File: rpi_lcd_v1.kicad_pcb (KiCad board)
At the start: 2 copper layers, 43.5 x 53 mm, 21 parts, among them J1 RPI GPIO, P1 CONN_9

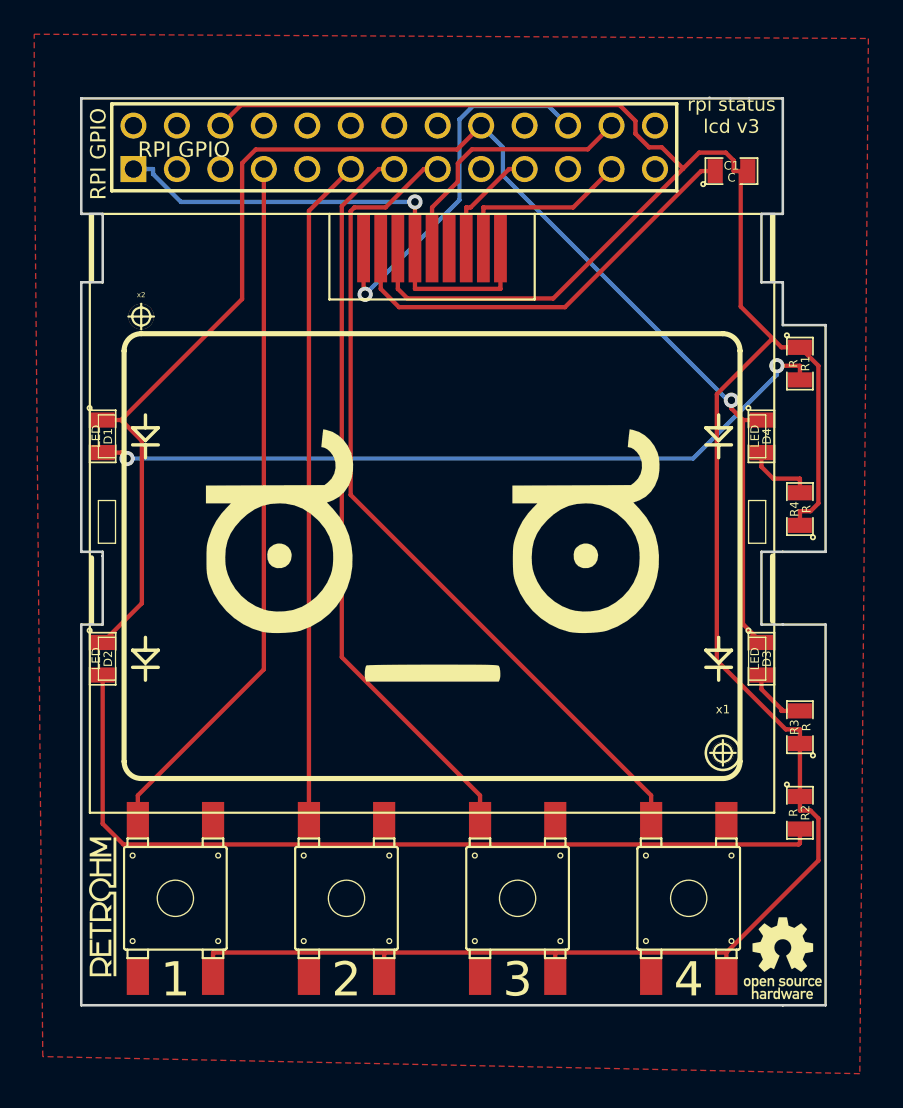
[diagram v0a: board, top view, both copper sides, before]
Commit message: Fixed d/c line, fixed LED orientation
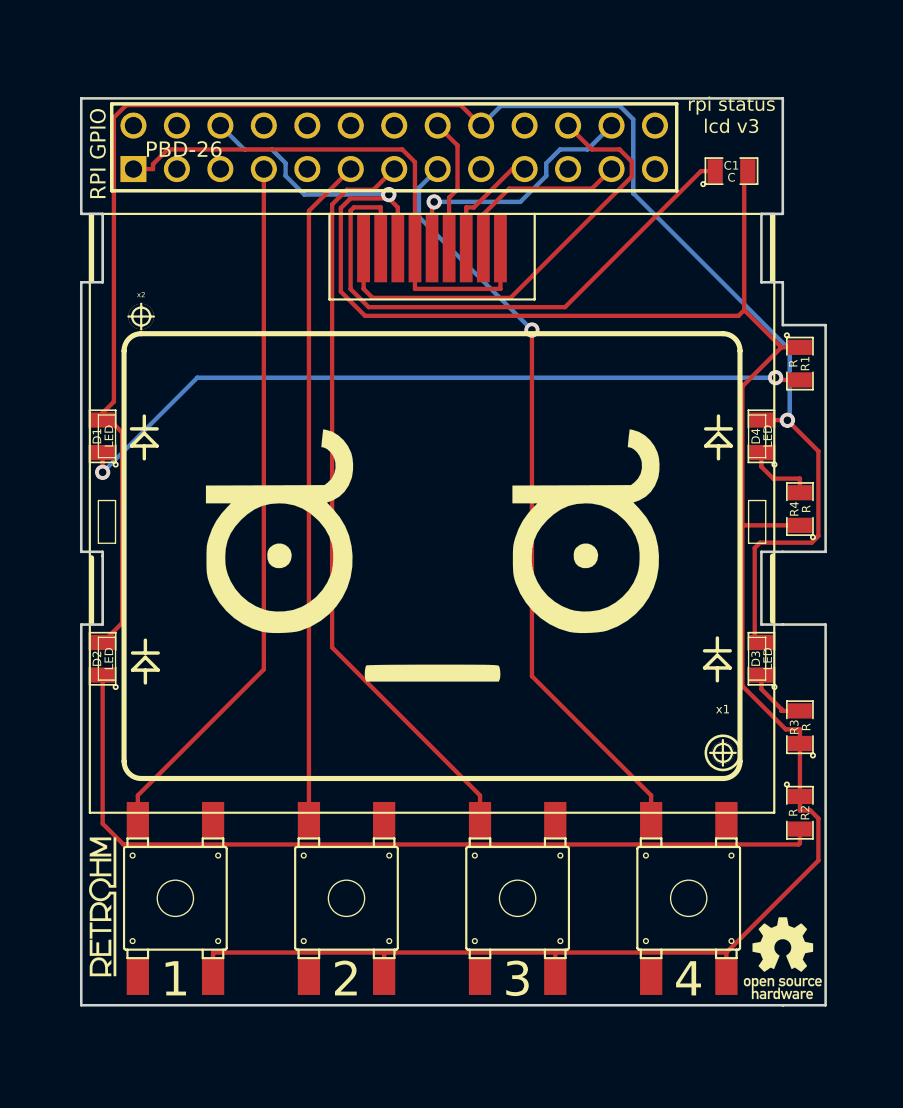
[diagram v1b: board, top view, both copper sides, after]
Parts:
- J1: value RPI GPIO -> PBD-26
- SW_1: value 1 -> FSM4JSMA-SMD
- SW_2: value 2 -> FSM4JSMA-SMD
- SW_3: value 3 -> FSM4JSMA-SMD
- SW_4: value 4 -> FSM4JSMA-SMD
- turned D1 to 90 degrees
- turned D2 to 90 degrees
- turned D3 to 90 degrees
- turned D4 to 90 degrees
- renumbered VAL to back_scaled
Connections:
- D1 pad 1: N-0000028 -> N-0000030
- D1 pad 2: N-0000031 -> N-0000027
- D2 pad 1: N-0000028 -> N-0000031
- D2 pad 2: N-0000032 -> N-0000027
- D3 pad 2: N-0000029 -> N-0000027
- D4 pad 1: N-0000028 -> N-0000029
- D4 pad 2: N-0000030 -> N-0000027
- J1 pad 10: (no net) -> N-0000018
- J1 pad 12: (no net) -> N-0000020
- J1 pad 14: (no net) -> N-0000013
- J1 pad 16: (no net) -> D_C
- J1 pad 17: (no net) -> N-0000011
- J1 pad 18: N-0000028 -> N-0000027
- J1 pad 2: (no net) -> N-0000021
- J1 pad 20: (no net) -> N-0000012
- J1 pad 21: (no net) -> N-0000019
- J1 pad 25: (no net) -> N-0000015
- J1 pad 26: (no net) -> N-000009
- J1 pad 3: (no net) -> N-0000022
- J1 pad 4: (no net) -> N-0000014
- J1 pad 5: (no net) -> N-0000023
- J1 pad 8: (no net) -> N-0000017
- J1 pad 9: (no net) -> N-0000010
- P1 pad 6: (no net) -> D_C
- R1 pad 2: N-0000031 -> N-0000030
- R2 pad 2: N-0000032 -> N-0000031
- R3 pad 2: N-0000029 -> N-0000028
- R4 pad 2: N-0000030 -> N-0000029
- SW_1 pad P$2: (no net) -> N-0000034
- SW_1 pad P$3: (no net) -> N-0000035
- SW_2 pad P$2: (no net) -> N-0000036
- SW_2 pad P$3: (no net) -> N-0000037
- SW_3 pad P$2: (no net) -> N-0000038
- SW_3 pad P$3: (no net) -> N-0000039
- SW_4 pad P$2: (no net) -> N-0000032
- SW_4 pad P$3: (no net) -> N-0000033
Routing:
- net N-0000027: track 0.00 -> 104.4 mm, vias 0 -> 1
- net N-0000028: track 86.5 -> 3.66 mm, vias 1 -> 0
- net N-0000032: track 50.8 -> 0.00 mm
- net N-0000030: track 4.19 -> 44.2 mm, vias 0 -> 2
- net GND: track 159.4 -> 140.3 mm, vias 0 -> 1
- net N-000007: track 25.7 -> 33.8 mm
- net D_C: track 0.00 -> 7.85 mm
- net N-0000031: track 44.3 -> 50.8 mm, vias 2 -> 0
- net SW_4: track 49.0 -> 44.1 mm, vias 0 -> 1
- net RST: track 22.4 -> 26.7 mm, vias 1 -> 0
- net +3.3V: track 29.9 -> 32.2 mm, vias 1 -> 0
- net SW_3: track 43.2 -> 44.0 mm
- net N-0000029: track 3.66 -> 4.19 mm
- net SCE: track 15.5 -> 15.4 mm, vias 0 -> 1
- removed copper zone on F.Cu, net GND

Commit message: Fixed back of board, plotted gerbers for oshpark order
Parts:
- removed back_scaled: back_scaled, back_scaled
- added VAL: bah, bah, F.Cu at (259.0, 141.4)
